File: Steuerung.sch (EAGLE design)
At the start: 15 parts

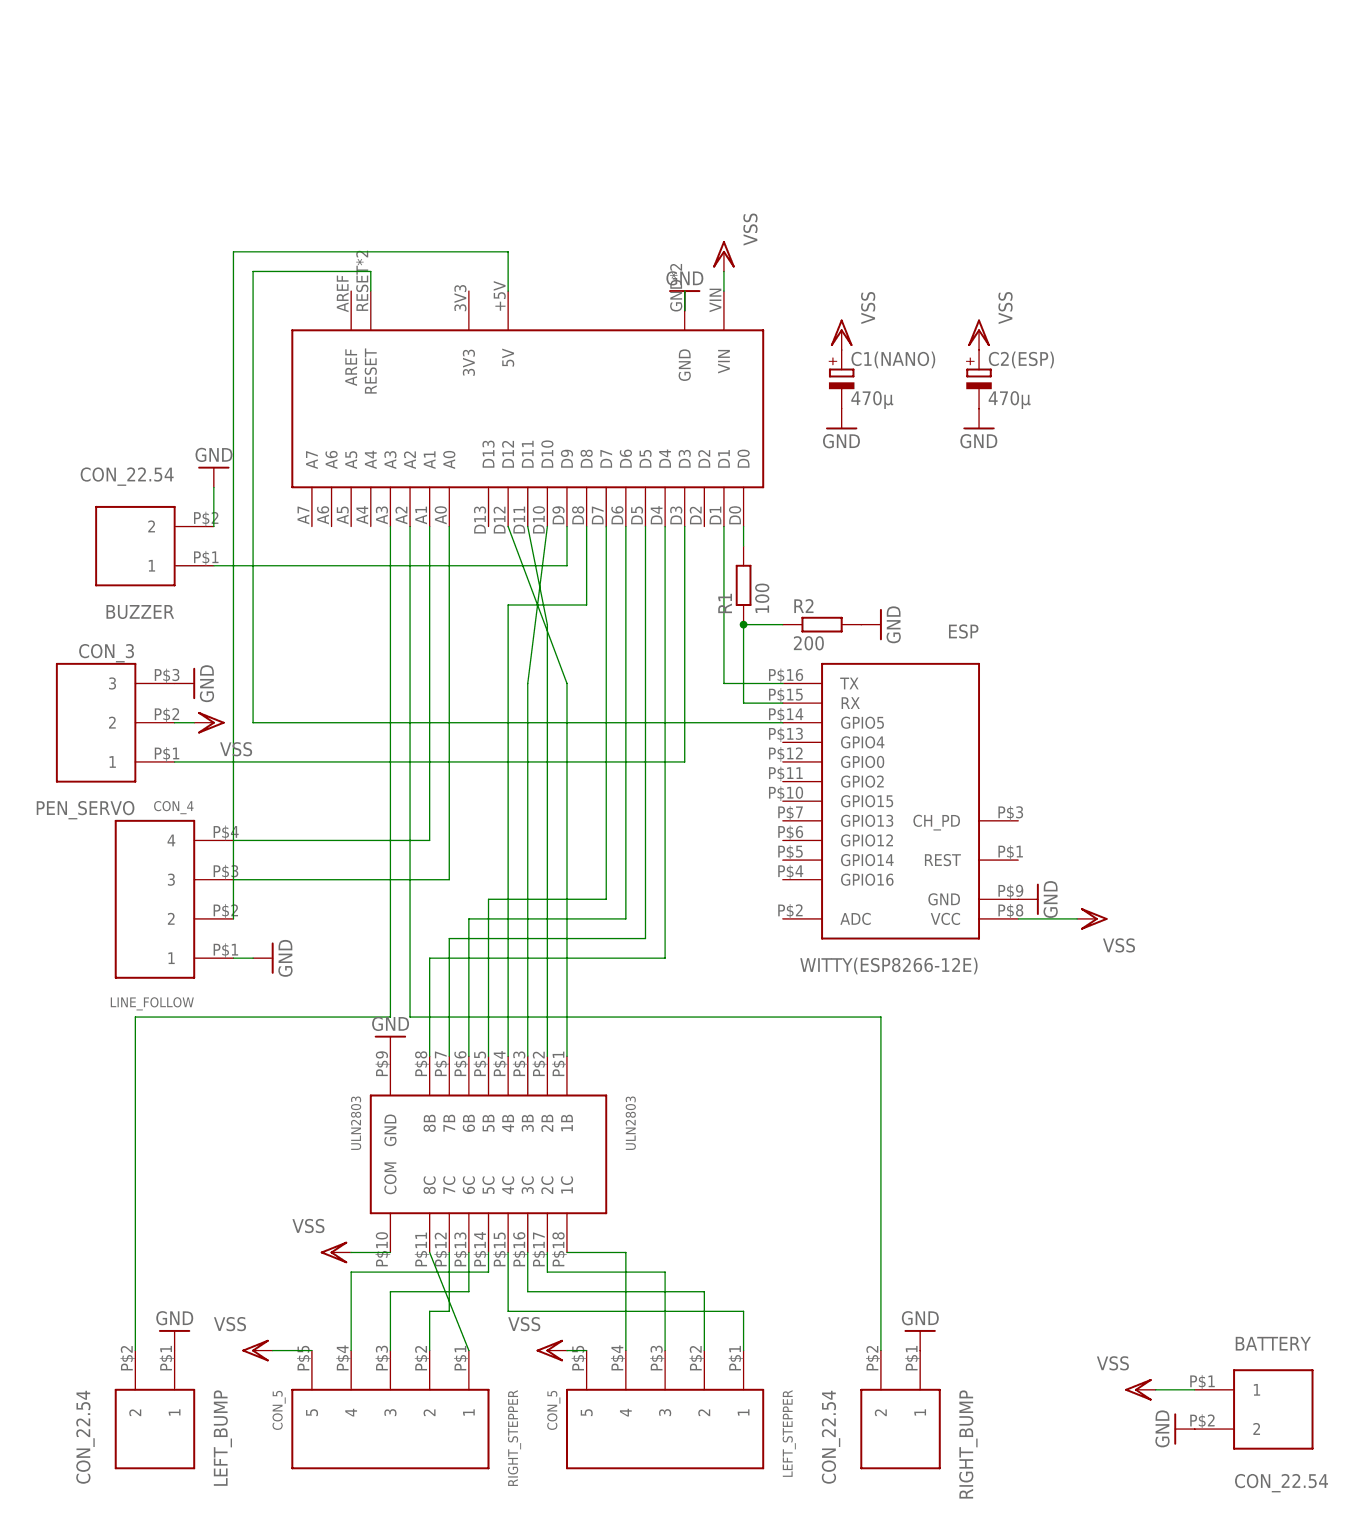
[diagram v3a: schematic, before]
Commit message: PCB resize, origin point fix
PCB compressed (Y-axis) to fit 2 PCBs on a 160x100cm Sheet.
Adjusted origin point in Y-Axis.
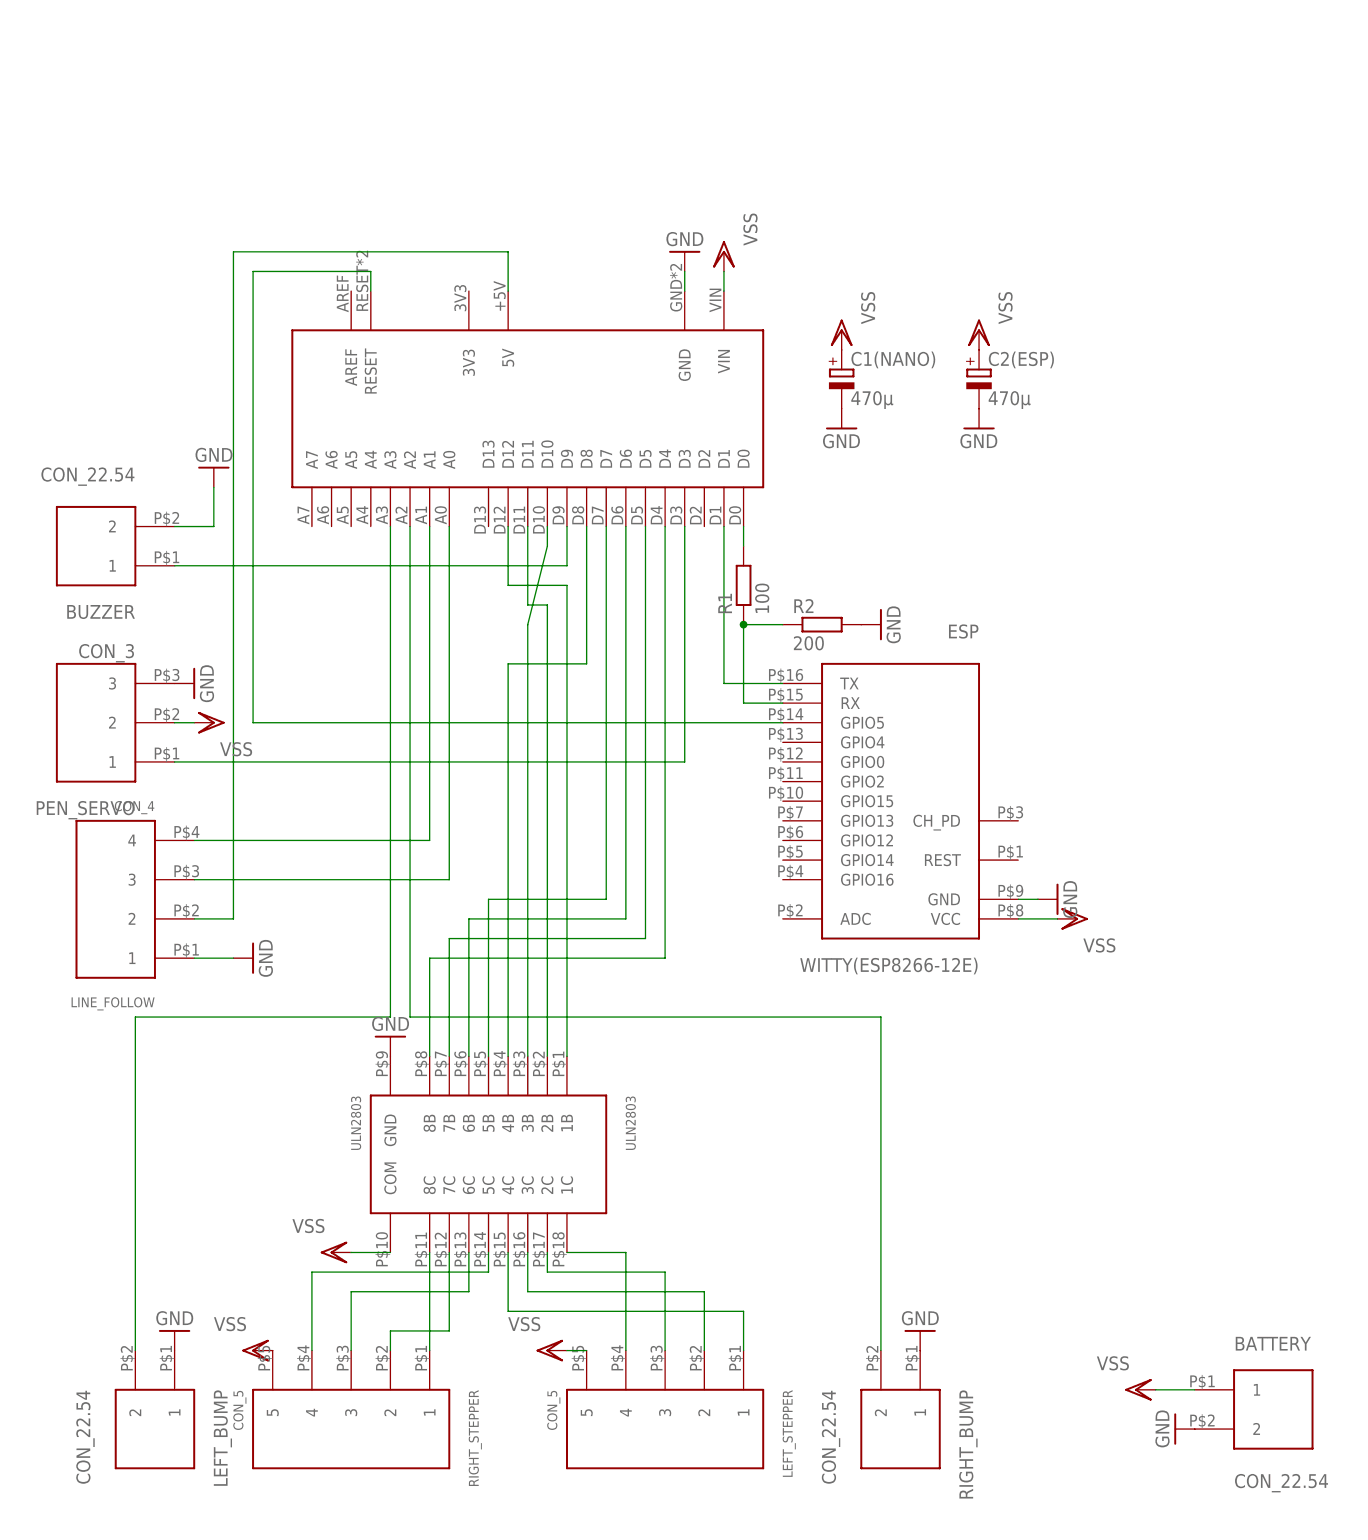
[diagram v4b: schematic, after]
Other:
- moved on the sheet: BUZZER, LINE_FOLLOW, RIGHT_STEPPER
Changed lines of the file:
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@@
 <?xml version="1.0" encoding="utf-8"?>
 <!DOCTYPE eagle SYSTEM "eagle.dtd">
-<eagle version="7.5.0">
+<eagle version="7.3.0">
 <drawing>
 <settings>
@@
 <instance part="WITTY(ESP8266-12E)" gate="G$1" x="73.66" y="73.66" rot="R180"/>
 <instance part="ULN2803" gate="G$1" x="20.32" y="27.94" rot="R270"/>
-<instance part="RIGHT_STEPPER" gate="G$1" x="7.62" y="-7.62" rot="R270"/>
+<instance part="RIGHT_STEPPER" gate="G$1" x="2.54" y="-7.62" rot="R270"/>
 <instance part="LEFT_STEPPER" gate="G$1" x="43.18" y="-7.62" rot="R270"/>
-<instance part="LINE_FOLLOW" gate="G$1" x="-22.86" y="60.96" rot="R180"/>
+<instance part="LINE_FOLLOW" gate="G$1" x="-27.94" y="60.96" rot="R180"/>
 <instance part="PEN_SERVO" gate="G$1" x="-30.48" y="83.82" rot="R180"/>
 <instance part="LEFT_BUMP" gate="G$1" x="-22.86" y="-7.62" rot="R270"/>
 <instance part="RIGHT_BUMP" gate="G$1" x="73.66" y="-7.62" rot="R270"/>
 <instance part="BATTERY" gate="G$1" x="121.92" y="-5.08"/>
-<instance part="BUZZER" gate="G$1" x="-25.4" y="106.68" rot="R180"/>
+<instance part="BUZZER" gate="G$1" x="-30.48" y="106.68" rot="R180"/>
 <instance part="R1" gate="G$1" x="53.34" y="101.6" rot="R90"/>
 <instance part="R2" gate="G$1" x="63.5" y="96.52"/>
 <instance part="GND1" gate="1" x="71.12" y="96.52" rot="R90"/>
-<instance part="GND2" gate="1" x="91.44" y="60.96" rot="R90"/>
+<instance part="GND2" gate="1" x="93.98" y="60.96" rot="R90"/>
 <instance part="GND3" gate="1" x="76.2" y="5.08" rot="R180"/>
 <instance part="GND4" gate="1" x="109.22" y="-7.62" rot="R270"/>
 <instance part="GND5" gate="1" x="-20.32" y="5.08" rot="R180"/>
 <instance part="GND6" gate="1" x="-15.24" y="116.84" rot="R180"/>
-<instance part="GND7" gate="1" x="-7.62" y="53.34" rot="R90"/>
+<instance part="GND7" gate="1" x="-10.16" y="53.34" rot="R90"/>
 <instance part="GND8" gate="1" x="-17.78" y="88.9" rot="R90"/>
-<instance part="GND9" gate="1" x="45.72" y="139.7" rot="R180"/>
+<instance part="GND9" gate="1" x="45.72" y="144.78" rot="R180"/>
 <instance part="GND10" gate="1" x="7.62" y="43.18" rot="R180"/>
 <instance part="VSS1" gate="G$1" x="104.14" y="-2.54" rot="R270"/>
-<instance part="VSS2" gate="G$1" x="99.06" y="58.42" rot="R90"/>
+<instance part="VSS2" gate="G$1" x="96.52" y="58.42" rot="R90"/>
 <instance part="VSS3" gate="G$1" x="50.8" y="144.78" rot="R180"/>
 <instance part="VSS4" gate="G$1" x="0" y="15.24" rot="R270"/>
@@
 <pinref part="WITTY(ESP8266-12E)" gate="G$1" pin="GND"/>
 <pinref part="GND2" gate="1" pin="GND"/>
+<wire x1="91.44" y1="60.96" x2="88.9" y2="60.96" width="0.1524" layer="91"/>
 </segment>
 <segment>
 <pinref part="ARDUINO_NANO" gate="G$1" pin="GND"/>
 <pinref part="GND9" gate="1" pin="GND"/>
-<wire x1="45.72" y1="139.7" x2="45.72" y2="137.16" width="0.1524" layer="91"/>
+<wire x1="45.72" y1="139.7" x2="45.72" y2="142.24" width="0.1524" layer="91"/>
 </segment>
 <segment>
@@
 <pinref part="BUZZER" gate="G$1" pin="2"/>
 <pinref part="GND6" gate="1" pin="GND"/>
+<wire x1="-20.32" y1="109.22" x2="-15.24" y2="109.22" width="0.1524" layer="91"/>
 <wire x1="-15.24" y1="109.22" x2="-15.24" y2="114.3" width="0.1524" layer="91"/>
 </segment>
@@
 <pinref part="LINE_FOLLOW" gate="G$1" pin="1"/>
 <pinref part="GND7" gate="1" pin="GND"/>
-<wire x1="-12.7" y1="53.34" x2="-10.16" y2="53.34" width="0.1524" layer="91"/>
+<wire x1="-17.78" y1="53.34" x2="-12.7" y2="53.34" width="0.1524" layer="91"/>
 </segment>
 <segment>
@@
 <segment>
 <pinref part="BUZZER" gate="G$1" pin="1"/>
-<wire x1="-15.24" y1="104.14" x2="30.48" y2="104.14" width="0.1524" layer="91"/>
+<wire x1="-20.32" y1="104.14" x2="30.48" y2="104.14" width="0.1524" layer="91"/>
 <pinref part="ARDUINO_NANO" gate="G$1" pin="D9"/>
 <wire x1="30.48" y1="104.14" x2="30.48" y2="109.22" width="0.1524" layer="91"/>
@@
 <wire x1="12.7" y1="109.22" x2="12.7" y2="68.58" width="0.1524" layer="91"/>
 <pinref part="LINE_FOLLOW" gate="G$1" pin="4"/>
-<wire x1="12.7" y1="68.58" x2="-12.7" y2="68.58" width="0.1524" layer="91"/>
+<wire x1="12.7" y1="68.58" x2="-17.78" y2="68.58" width="0.1524" layer="91"/>
 </segment>
 </net>
@@
 <segment>
 <pinref part="LINE_FOLLOW" gate="G$1" pin="3"/>
-<wire x1="-12.7" y1="63.5" x2="15.24" y2="63.5" width="0.1524" layer="91"/>
+<wire x1="-17.78" y1="63.5" x2="15.24" y2="63.5" width="0.1524" layer="91"/>
 <pinref part="ARDUINO_NANO" gate="G$1" pin="A0"/>
 <wire x1="15.24" y1="63.5" x2="15.24" y2="109.22" width="0.1524" layer="91"/>
@@
 <segment>
 <pinref part="LINE_FOLLOW" gate="G$1" pin="2"/>
+<wire x1="-17.78" y1="58.42" x2="-12.7" y2="58.42" width="0.1524" layer="91"/>
 <wire x1="-12.7" y1="58.42" x2="-12.7" y2="144.78" width="0.1524" layer="91"/>
 <wire x1="-12.7" y1="144.78" x2="22.86" y2="144.78" width="0.1524" layer="91"/>
@@
 <pinref part="WITTY(ESP8266-12E)" gate="G$1" pin="VCC"/>
 <pinref part="VSS2" gate="G$1" pin="VSS"/>
-<wire x1="88.9" y1="58.42" x2="96.52" y2="58.42" width="0.1524" layer="91"/>
+<wire x1="88.9" y1="58.42" x2="93.98" y2="58.42" width="0.1524" layer="91"/>
 </segment>
 <segment>
@@
 <pinref part="RIGHT_STEPPER" gate="G$1" pin="5"/>
 <pinref part="VSS9" gate="G$1" pin="VSS"/>
-<wire x1="-7.62" y1="2.54" x2="-2.54" y2="2.54" width="0.1524" layer="91"/>
 </segment>
 <segment>
@@
 <segment>
 <pinref part="ARDUINO_NANO" gate="G$1" pin="D8"/>
-<wire x1="33.02" y1="109.22" x2="33.02" y2="99.06" width="0.1524" layer="91"/>
+<wire x1="33.02" y1="109.22" x2="33.02" y2="91.44" width="0.1524" layer="91"/>
 <pinref part="ULN2803" gate="G$1" pin="4B"/>
-<wire x1="33.02" y1="99.06" x2="22.86" y2="99.06" width="0.1524" layer="91"/>
-<wire x1="22.86" y1="99.06" x2="22.86" y2="40.64" width="0.1524" layer="91"/>
+<wire x1="33.02" y1="91.44" x2="22.86" y2="91.44" width="0.1524" layer="91"/>
+<wire x1="22.86" y1="91.44" x2="22.86" y2="40.64" width="0.1524" layer="91"/>
 </segment>
 </net>
@@
 <pinref part="ULN2803" gate="G$1" pin="5C"/>
 <wire x1="20.32" y1="15.24" x2="20.32" y2="12.7" width="0.1524" layer="91"/>
-<wire x1="20.32" y1="12.7" x2="2.54" y2="12.7" width="0.1524" layer="91"/>
+<wire x1="20.32" y1="12.7" x2="-2.54" y2="12.7" width="0.1524" layer="91"/>
 <pinref part="RIGHT_STEPPER" gate="G$1" pin="4"/>
-<wire x1="2.54" y1="12.7" x2="2.54" y2="2.54" width="0.1524" layer="91"/>
+<wire x1="-2.54" y1="12.7" x2="-2.54" y2="2.54" width="0.1524" layer="91"/>
 </segment>
 </net>
@@
 <wire x1="17.78" y1="15.24" x2="17.78" y2="10.16" width="0.1524" layer="91"/>
 <pinref part="RIGHT_STEPPER" gate="G$1" pin="3"/>
-<wire x1="17.78" y1="10.16" x2="7.62" y2="10.16" width="0.1524" layer="91"/>
-<wire x1="7.62" y1="10.16" x2="7.62" y2="2.54" width="0.1524" layer="91"/>
+<wire x1="17.78" y1="10.16" x2="2.54" y2="10.16" width="0.1524" layer="91"/>
+<wire x1="2.54" y1="10.16" x2="2.54" y2="2.54" width="0.1524" layer="91"/>
 </segment>
 </net>
@@
 <segment>
 <pinref part="ULN2803" gate="G$1" pin="7C"/>
-<wire x1="15.24" y1="15.24" x2="15.24" y2="7.62" width="0.1524" layer="91"/>
+<wire x1="15.24" y1="15.24" x2="15.24" y2="5.08" width="0.1524" layer="91"/>
 <pinref part="RIGHT_STEPPER" gate="G$1" pin="2"/>
-<wire x1="15.24" y1="7.62" x2="12.7" y2="7.62" width="0.1524" layer="91"/>
-<wire x1="12.7" y1="7.62" x2="12.7" y2="2.54" width="0.1524" layer="91"/>
+<wire x1="15.24" y1="5.08" x2="7.62" y2="5.08" width="0.1524" layer="91"/>
+<wire x1="7.62" y1="5.08" x2="7.62" y2="2.54" width="0.1524" layer="91"/>
 </segment>
 </net>
@@
 <pinref part="ULN2803" gate="G$1" pin="8C"/>
 <pinref part="RIGHT_STEPPER" gate="G$1" pin="1"/>
-<wire x1="12.7" y1="15.24" x2="17.78" y2="2.54" width="0.1524" layer="91"/>
+<wire x1="12.7" y1="15.24" x2="12.7" y2="2.54" width="0.1524" layer="91"/>
 </segment>
 </net>
@@
 <segment>
 <pinref part="ULN2803" gate="G$1" pin="3B"/>
-<wire x1="25.4" y1="40.64" x2="25.4" y2="88.9" width="0.1524" layer="91"/>
+<wire x1="25.4" y1="40.64" x2="25.4" y2="96.52" width="0.1524" layer="91"/>
 <pinref part="ARDUINO_NANO" gate="G$1" pin="D10"/>
-<wire x1="25.4" y1="88.9" x2="27.94" y2="109.22" width="0.1524" layer="91"/>
+<wire x1="25.4" y1="96.52" x2="27.94" y2="106.68" width="0.1524" layer="91"/>
+<wire x1="27.94" y1="106.68" x2="27.94" y2="109.22" width="0.1524" layer="91"/>
 </segment>
 </net>
@@
 <segment>
 <pinref part="ULN2803" gate="G$1" pin="2B"/>
-<wire x1="27.94" y1="40.64" x2="27.94" y2="96.52" width="0.1524" layer="91"/>
+<wire x1="27.94" y1="40.64" x2="27.94" y2="99.06" width="0.1524" layer="91"/>
 <pinref part="ARDUINO_NANO" gate="G$1" pin="D11"/>
-<wire x1="27.94" y1="96.52" x2="25.4" y2="109.22" width="0.1524" layer="91"/>
+<wire x1="27.94" y1="99.06" x2="25.4" y2="99.06" width="0.1524" layer="91"/>
+<wire x1="25.4" y1="99.06" x2="25.4" y2="109.22" width="0.1524" layer="91"/>
 </segment>
 </net>
@@
 <segment>
 <pinref part="ULN2803" gate="G$1" pin="1B"/>
-<wire x1="30.48" y1="40.64" x2="30.48" y2="88.9" width="0.1524" layer="91"/>
+<wire x1="30.48" y1="40.64" x2="30.48" y2="101.6" width="0.1524" layer="91"/>
 <pinref part="ARDUINO_NANO" gate="G$1" pin="D12"/>
-<wire x1="30.48" y1="88.9" x2="22.86" y2="109.22" width="0.1524" layer="91"/>
-</segment>
-</net>
+<wire x1="30.48" y1="101.6" x2="22.86" y2="101.6" width="0.1524" layer="91"/>
+<wire x1="22.86" y1="101.6" x2="22.86" y2="109.22" width="0.1524" layer="91"/>
+</segment>
+</net>

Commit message: PCB Resize
Made the PCB even smaller to be millable on the Proxxon MF 70.
This is the Version currently being tested in the Lab.
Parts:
- added R4: 0, rcl-2:R-EU_R1206
- WITTY(ESP8266-12E): value ESP -> ESPWITTY; device pcaroli:ESP -> pcaroli:ESPWITTY
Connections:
- new net N$29: R4.2, ULN2803.GND
- net GND: now also R4.1; no longer ULN2803.GND
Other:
- moved on the sheet: BATTERY
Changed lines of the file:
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@@
 <parts>
 <part name="ARDUINO_NANO" library="pcaroli" deviceset="ARDUINO_NANO" device=""/>
-<part name="WITTY(ESP8266-12E)" library="pcaroli" deviceset="ESP" device=""/>
+<part name="WITTY(ESP8266-12E)" library="pcaroli" deviceset="ESP" device="WITTY"/>
 <part name="ULN2803" library="pcaroli" deviceset="ULN2803" device=""/>
 <part name="RIGHT_STEPPER" library="pcaroli" deviceset="CON_5" device=""/>
@@
 <part name="GND12" library="supply1" deviceset="GND" device=""/>
 <part name="VSS9" library="supply1" deviceset="VSS" device=""/>
+<part name="R4" library="rcl-2" deviceset="R-EU_" device="R1206" value="0"/>
 </parts>
 <sheets>
@@
 <instance part="LEFT_BUMP" gate="G$1" x="-22.86" y="-7.62" rot="R270"/>
 <instance part="RIGHT_BUMP" gate="G$1" x="73.66" y="-7.62" rot="R270"/>
-<instance part="BATTERY" gate="G$1" x="121.92" y="-5.08"/>
+<instance part="BATTERY" gate="G$1" x="7.62" y="165.1"/>
 <instance part="BUZZER" gate="G$1" x="-30.48" y="106.68" rot="R180"/>
 <instance part="R1" gate="G$1" x="53.34" y="101.6" rot="R90"/>
@@
 <instance part="GND2" gate="1" x="93.98" y="60.96" rot="R90"/>
 <instance part="GND3" gate="1" x="76.2" y="5.08" rot="R180"/>
-<instance part="GND4" gate="1" x="109.22" y="-7.62" rot="R270"/>
+<instance part="GND4" gate="1" x="-5.08" y="162.56" rot="R270"/>
 <instance part="GND5" gate="1" x="-20.32" y="5.08" rot="R180"/>
 <instance part="GND6" gate="1" x="-15.24" y="116.84" rot="R180"/>
@@
 <instance part="GND8" gate="1" x="-17.78" y="88.9" rot="R90"/>
 <instance part="GND9" gate="1" x="45.72" y="144.78" rot="R180"/>
-<instance part="GND10" gate="1" x="7.62" y="43.18" rot="R180"/>
-<instance part="VSS1" gate="G$1" x="104.14" y="-2.54" rot="R270"/>
+<instance part="GND10" gate="1" x="-12.7" y="40.64" rot="R270"/>
+<instance part="VSS1" gate="G$1" x="-10.16" y="167.64" rot="R270"/>
 <instance part="VSS2" gate="G$1" x="96.52" y="58.42" rot="R90"/>
 <instance part="VSS3" gate="G$1" x="50.8" y="144.78" rot="R180"/>
@@
 <instance part="GND12" gate="1" x="66.04" y="121.92"/>
 <instance part="VSS9" gate="G$1" x="-10.16" y="2.54" rot="R270"/>
+<instance part="R4" gate="G$1" x="-2.54" y="40.64"/>
 </instances>
 <busses>
 </busses>
 <nets>
-<net name="N$17" class="0">
-<segment>
-<pinref part="LEFT_BUMP" gate="G$1" pin="2"/>
-<wire x1="-25.4" y1="2.54" x2="-25.4" y2="45.72" width="0.1524" layer="91"/>
-<wire x1="-25.4" y1="45.72" x2="7.62" y2="45.72" width="0.1524" layer="91"/>
-<pinref part="ARDUINO_NANO" gate="G$1" pin="A3"/>
-<wire x1="7.62" y1="45.72" x2="7.62" y2="109.22" width="0.1524" layer="91"/>
-</segment>
-</net>
 <net name="N$18" class="0">
 <segment>
@@
 </segment>
 <segment>
-<pinref part="ULN2803" gate="G$1" pin="GND"/>
+<pinref part="R4" gate="G$1" pin="1"/>
 <pinref part="GND10" gate="1" pin="GND"/>
+<wire x1="-10.16" y1="40.64" x2="-7.62" y2="40.64" width="0.1524" layer="91"/>
 </segment>
 <segment>
@@
 </segment>
 </net>
-<net name="N$27" class="0">
-<segment>
-<pinref part="LINE_FOLLOW" gate="G$1" pin="2"/>
-<wire x1="-17.78" y1="58.42" x2="-12.7" y2="58.42" width="0.1524" layer="91"/>
-<wire x1="-12.7" y1="58.42" x2="-12.7" y2="144.78" width="0.1524" layer="91"/>
+<net name="N$30" class="0">
+<segment>
 <wire x1="-12.7" y1="144.78" x2="22.86" y2="144.78" width="0.1524" layer="91"/>
 <pinref part="ARDUINO_NANO" gate="G$1" pin="5V"/>
 <wire x1="22.86" y1="144.78" x2="22.86" y2="139.7" width="0.1524" layer="91"/>
+<wire x1="-12.7" y1="58.42" x2="-12.7" y2="144.78" width="0.1524" layer="91"/>
+<pinref part="LINE_FOLLOW" gate="G$1" pin="2"/>
+<wire x1="-17.78" y1="58.42" x2="-12.7" y2="58.42" width="0.1524" layer="91"/>
 </segment>
 </net>
@@
 <pinref part="BATTERY" gate="G$1" pin="1"/>
 <pinref part="VSS1" gate="G$1" pin="VSS"/>
-<wire x1="106.68" y1="-2.54" x2="111.76" y2="-2.54" width="0.1524" layer="91"/>
+<wire x1="-7.62" y1="167.64" x2="-2.54" y2="167.64" width="0.1524" layer="91"/>
 </segment>
 <segment>
@@
 </segment>
 </net>
+<net name="N$28" class="0">
+<segment>
+<pinref part="LEFT_BUMP" gate="G$1" pin="2"/>
+<wire x1="-25.4" y1="2.54" x2="-25.4" y2="45.72" width="0.1524" layer="91"/>
+<pinref part="ARDUINO_NANO" gate="G$1" pin="A3"/>
+<wire x1="7.62" y1="45.72" x2="7.62" y2="109.22" width="0.1524" layer="91"/>
+<wire x1="-25.4" y1="45.72" x2="7.62" y2="45.72" width="0.1524" layer="91"/>
+</segment>
+</net>
+<net name="N$29" class="0">
+<segment>
+<pinref part="ULN2803" gate="G$1" pin="GND"/>
+<pinref part="R4" gate="G$1" pin="2"/>
+<wire x1="2.54" y1="40.64" x2="7.62" y2="40.64" width="0.1524" layer="91"/>
+</segment>
+</net>
